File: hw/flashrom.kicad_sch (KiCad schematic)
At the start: 14 parts, among them J1 Conn_01x04_Pin, J2 Conn_01x03_Pin, J3 Conn_01x04_Pin, U1 29F800-TSOP, U2 Kickstart_Socket_A4000

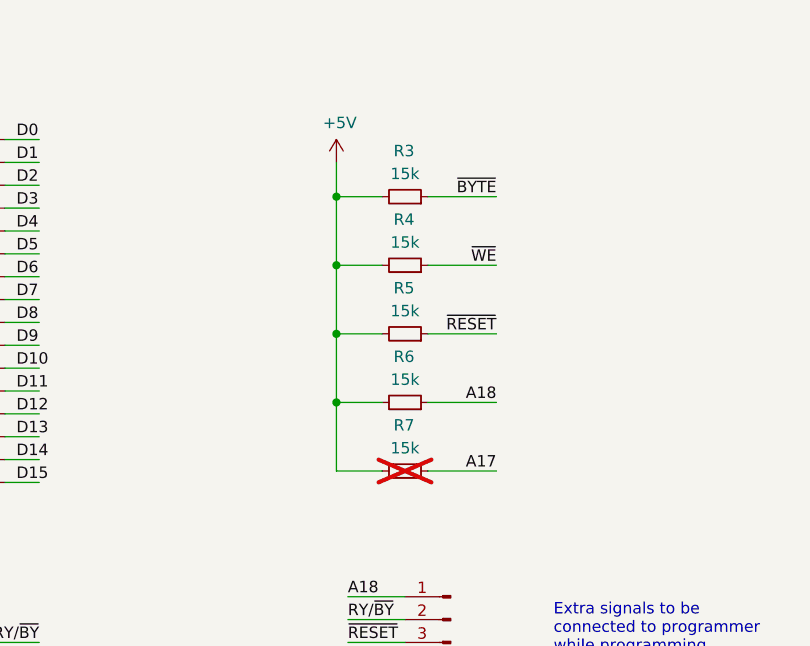
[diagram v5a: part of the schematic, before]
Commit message: increase pull-ups to 18k, the value actually used in the protos
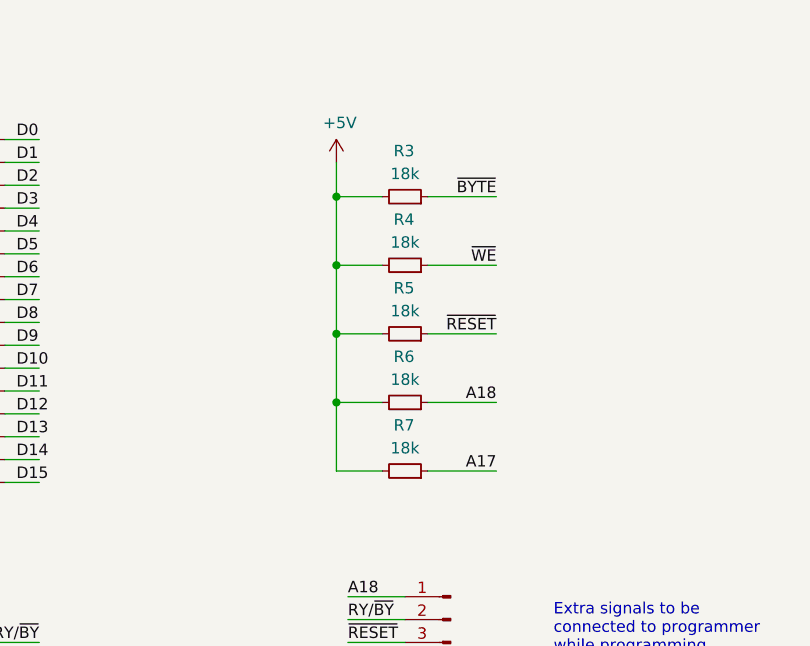
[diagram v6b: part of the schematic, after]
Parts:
- R3, R4, R5, R6: value 15k -> 18k
- R7: value 15k -> 18k; now fitted; now in the parts list
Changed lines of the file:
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@@
       (effects (font (size 1.27 1.27)) (justify left))
     )
-    (property "Value" "15k" (at 232.41 67.31 90)
+    (property "Value" "18k" (at 232.41 67.31 90)
       (effects (font (size 1.27 1.27)))
     )
@@
       (effects (font (size 1.27 1.27)) (justify left))
     )
-    (property "Value" "15k" (at 232.41 74.93 90)
+    (property "Value" "18k" (at 232.41 74.93 90)
       (effects (font (size 1.27 1.27)))
     )
@@
   )
   (symbol (lib_id "Device:R_Small") (at 232.41 92.71 270) (mirror x) (unit 1)
-    (in_bom no) (on_board yes) (dnp yes)
+    (in_bom yes) (on_board yes) (dnp no)
     (property "Reference" "R7" (at 231.14 87.63 90)
       (effects (font (size 1.27 1.27)) (justify left))
     )
-    (property "Value" "15k" (at 232.41 90.17 90)
+    (property "Value" "18k" (at 232.41 90.17 90)
       (effects (font (size 1.27 1.27)))
     )
@@
       (effects (font (size 1.27 1.27)) (justify left))
     )
-    (property "Value" "15k" (at 232.41 59.69 90)
+    (property "Value" "18k" (at 232.41 59.69 90)
       (effects (font (size 1.27 1.27)))
     )
@@
       (effects (font (size 1.27 1.27)) (justify left))
     )
-    (property "Value" "15k" (at 232.41 82.55 90)
-      (effects (font (size 1.27 1.27)))
-    )
+    (property "Value" "18k" (at 232.41 82.55 90)
+      (effects (font (size 1.27 1.27)))
+    )
